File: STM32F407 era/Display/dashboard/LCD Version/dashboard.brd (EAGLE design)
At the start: 200 x 75.1 mm, 61 parts, among them U1 CAT4238TD-GT3

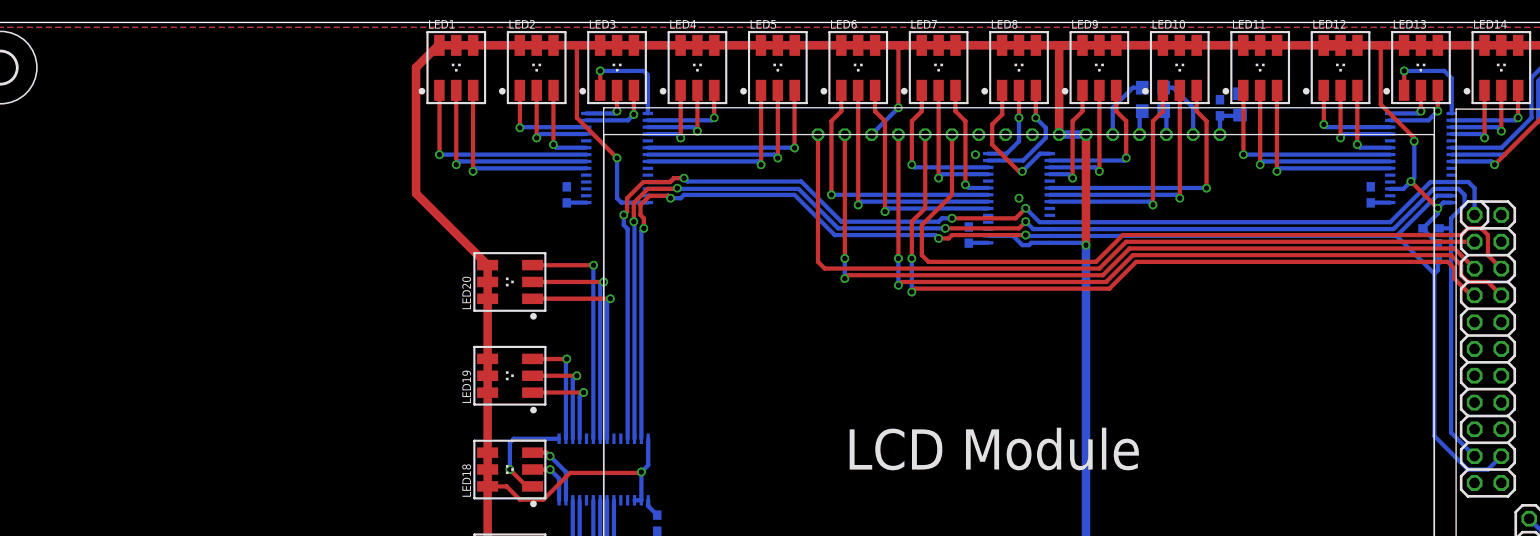
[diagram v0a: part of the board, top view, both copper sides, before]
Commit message: added dashboard control buttons
added buttons to add functionality to the LCD panel
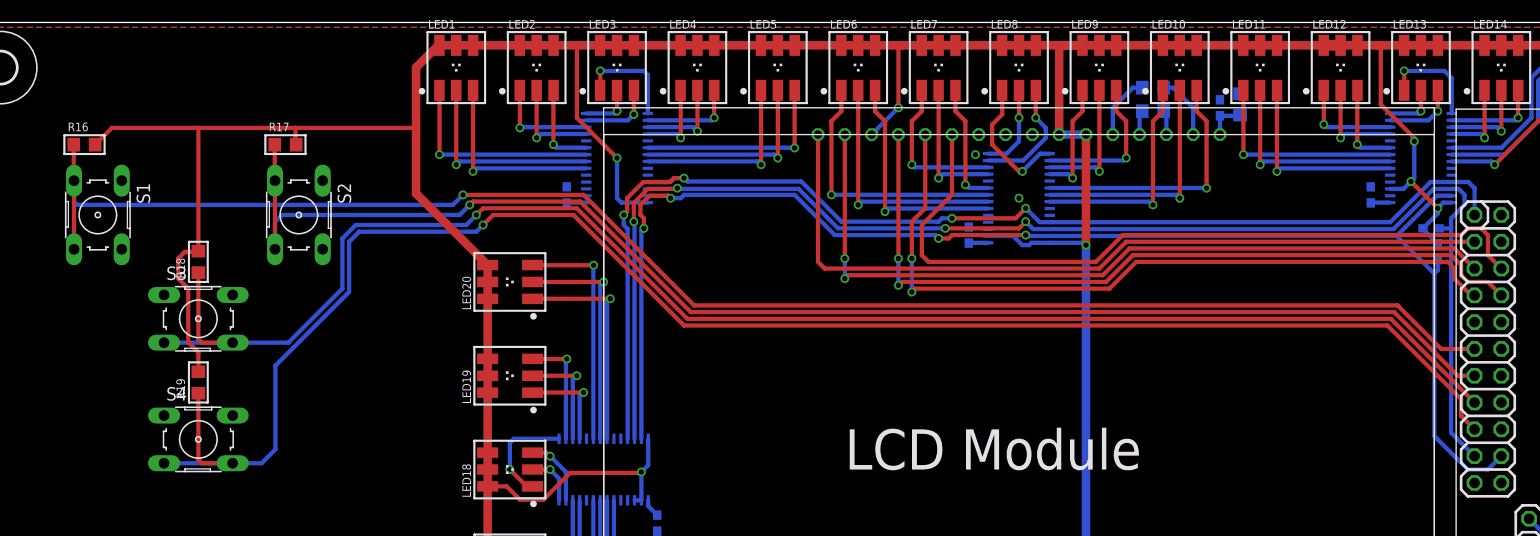
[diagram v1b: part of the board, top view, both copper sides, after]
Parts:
- added R16, R17, R18, R19: 500, microbuilder:_0805
- added S1, S2, S3, S4: (no value), switch-omron:B3F-10XX
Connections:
- new net SW1: R16.1, S1.3, S1.4, U$1.P$11
- new net SW2: R17.1, S2.3, S2.4, U$1.P$13
- new net SW3: R18.1, S3.3, S3.4, U$1.P$15
- new net SW4: R19.1, S4.3, S4.4, U$1.P$17
- net 3.3V: now also R16.2, R17.2, R18.2, R19.2
- net GND: now also S1.1, S1.2, S2.1, S2.2, S3.1, S3.2, S4.1, S4.2
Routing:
- net SW4: track 0.00 -> 160.5 mm, vias 0 -> 1
- net SW1: track 0.00 -> 151.3 mm, vias 0 -> 1
- net SW3: track 0.00 -> 149.6 mm, vias 0 -> 1
- net SW2: track 0.00 -> 133.9 mm, vias 0 -> 1
- net 3.3V: track 469.0 -> 527.1 mm

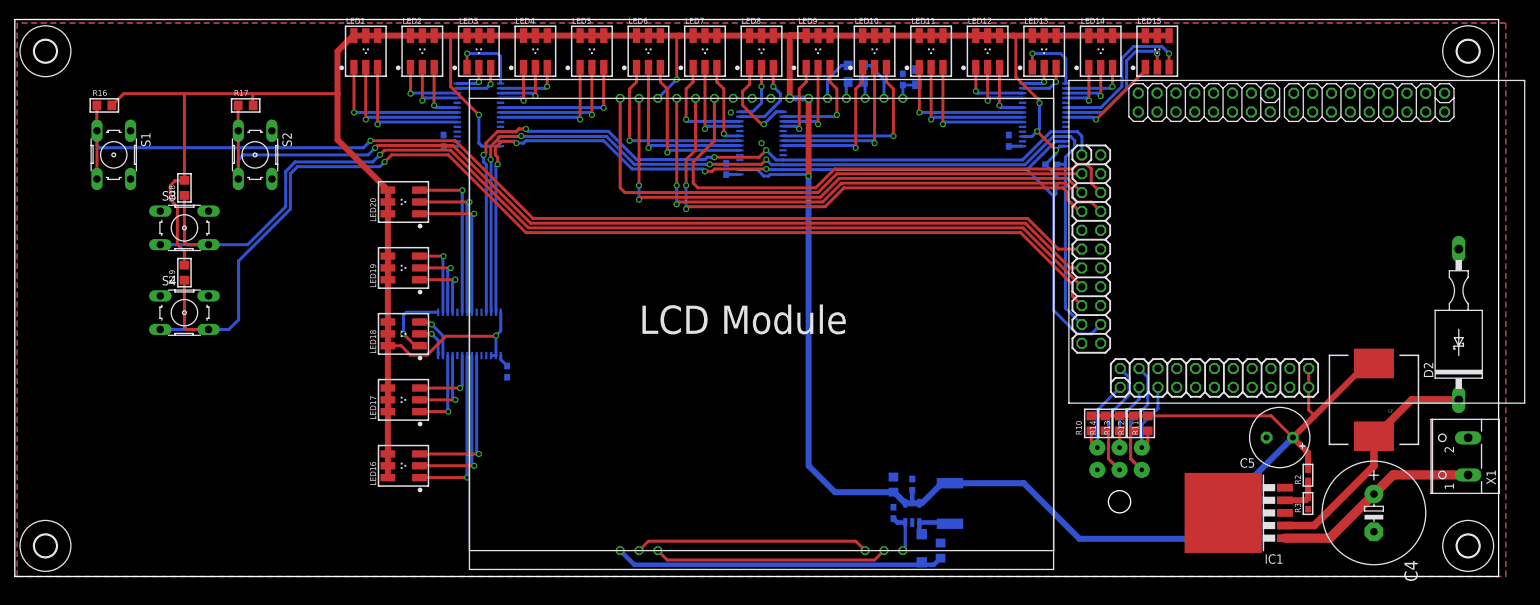
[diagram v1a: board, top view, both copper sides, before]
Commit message: added hardware debounce circuit to buttons
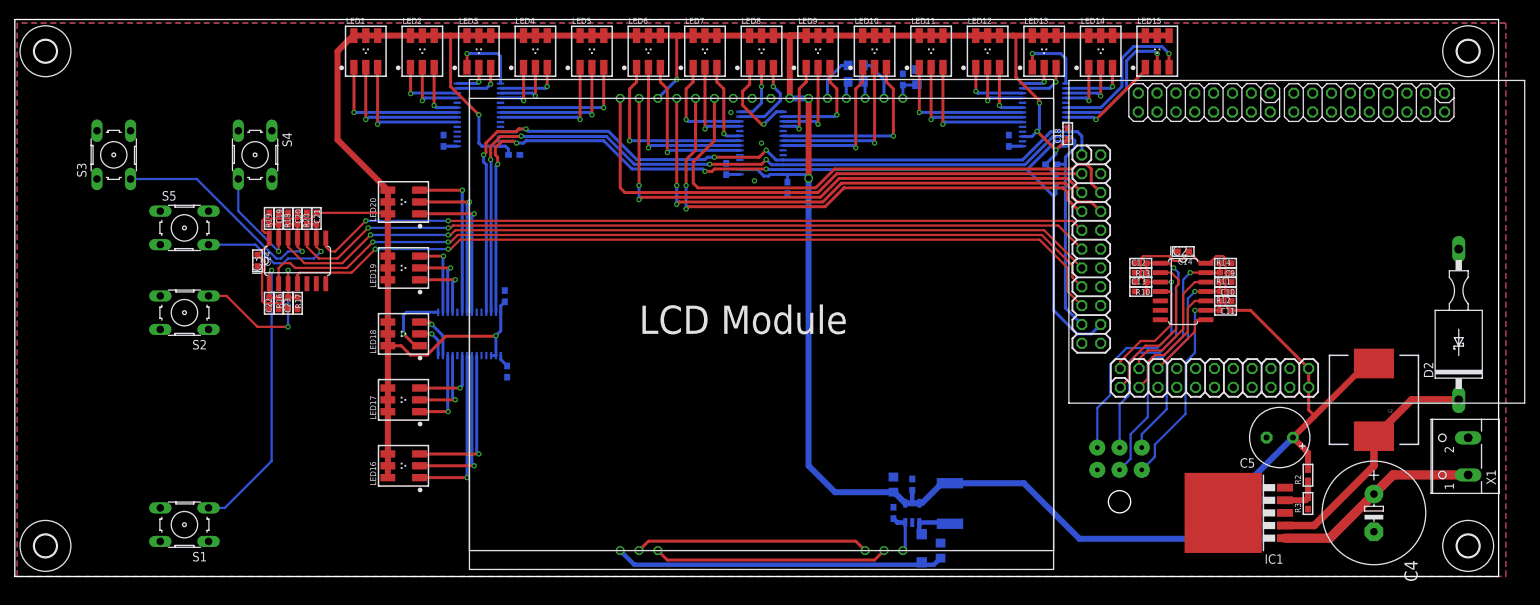
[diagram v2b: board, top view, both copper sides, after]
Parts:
- added C10, C11, C12, C13, C14, C15, C16, C17, C18, C19, C20, C21, C22, C23, C24, C9: 100n, microbuilder:_0603
- added IC2, IC3: 74HC14D, 74xx-eu:SO14
- added R20: 500, microbuilder:_0603
- added S5: (no value), switch-omron:B3F-10XX
- R10, R11, R12, R13, R14, R16, R17, R18, R19: device microbuilder:_0805 -> microbuilder:_0603
- moved S1 50.7 mm to (22.5, 6.03), turned to 180 degrees
- moved R16 34.7 mm to (34.0, 35.9), turned to 270 degrees
- moved R17 27.3 mm to (36.5, 35.9), turned to 270 degrees
- moved R14 26.0 mm to (162.9, 40.0), turned to 0 degrees
- moved S2 23.3 mm to (22.5, 34.6), turned to 180 degrees
- moved S4 23.3 mm to (32.1, 55.9), turned to 270 degrees
- moved R13 21.8 mm to (151.4, 41.3), turned to 180 degrees
- moved R11 20.6 mm to (162.9, 37.5), turned to 0 degrees
- moved R10 20.2 mm to (151.4, 38.7), turned to 180 degrees
- moved R12 19.6 mm to (162.9, 34.9), turned to 0 degrees
- moved R18 15.8 mm to (37.8, 47.3)
- moved R19 14.6 mm to (35.2, 47.3)
- moved S3 13.7 mm to (13.0, 55.9), turned to 90 degrees
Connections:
- new net BTN1S: IC2.2, U$1.P$23
- new net BTN2S: IC2.4, U$1.P$24
- new net BTN3S: IC2.10, U$1.P$25
- new net BTN4S: IC2.12, U$1.P$26
- new net BTN5S: IC2.8, U$1.P$28
- new net SW1S: IC3.2, U$1.P$15
- new net SW2S: IC3.4, U$1.P$17
- new net SW3S: IC3.10, U$1.P$11
- new net SW4S: IC3.12, U$1.P$13
- new net SW5: C21.2, IC3.9, R20.1, S5.3, S5.4
- new net SW5S: IC3.8, U$1.P$9
- net 3.3V: now also C14.1, C15.1, C16.1, C17.1, C18.1, C24.1, IC2.14, IC3.14, R20.2
- net BTN1: now also C12.2, IC2.1, R13.1, U$42.PIN4; no longer R10.1, U$1.P$23, U$42.PIN2
- net BTN2: now also C13.2, IC2.3, R10.1, U$42.PIN2; no longer R14.1, U$1.P$24, U$42.PIN3
- net BTN3: now also C10.2, IC2.11, R11.1, U$42.PIN6; no longer R13.1, U$1.P$25, U$42.PIN4
- net BTN4: now also C9.2, IC2.13, R14.1, U$42.PIN3; no longer R12.1, U$1.P$26, U$42.PIN5
- net BTN5: now also C11.2, IC2.9, R12.1, U$42.PIN5; no longer R11.1, U$1.P$27, U$42.PIN6
- net GND: now also C10.1, C11.1, C12.1, C13.1, C14.2, C15.2, C16.2, C17.2, C18.2, C19.1, C20.1, C21.1, C22.1, C23.1, C24.2, C9.1, IC2.5, IC2.7, IC3.5, IC3.7, S5.1, S5.2
- net SW1: now also C22.2, IC3.1; no longer U$1.P$11
- net SW2: now also C23.2, IC3.3; no longer U$1.P$13
- net SW3: now also C20.2, IC3.11; no longer U$1.P$15
- net SW4: now also C19.2, IC3.13; no longer U$1.P$17
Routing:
- net SW4: track 160.5 -> 17.0 mm
- net SW1S: track 0.00 -> 116.6 mm, vias 0 -> 2
- net SW3: track 149.6 -> 33.2 mm
- net SW2S: track 0.00 -> 114.4 mm, vias 0 -> 2
- net SW4S: track 0.00 -> 113.0 mm, vias 0 -> 2
- net SW3S: track 0.00 -> 109.4 mm, vias 0 -> 2
- net SW1: track 151.3 -> 41.9 mm
- net SW2: track 133.9 -> 25.0 mm, vias 1 -> 2
- net SW5S: track 0.00 -> 105.6 mm, vias 0 -> 2
- net BTN1: track 12.0 -> 34.7 mm, vias 0 -> 1
- net SW5: track 0.00 -> 22.1 mm, vias 0 -> 1
- net BTN1S: track 0.00 -> 21.7 mm
- net BTN5: track 11.6 -> 29.1 mm, vias 0 -> 1
- net BTN4S: track 0.00 -> 17.4 mm
- net BTN3: track 11.5 -> 28.6 mm, vias 0 -> 1
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
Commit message: small cosmic changes
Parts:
- moved S1 24.4 mm to (22.9, 30.5), turned to 0 degrees
- moved S5 15.9 mm to (22.9, 61.9)
- moved S2 10.8 mm to (22.9, 45.4), turned to 0 degrees
- moved S3 2.73 mm to (14.6, 53.7)
- moved S4 2.42 mm to (31.1, 53.7)
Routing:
- net SW5: track 22.1 -> 39.8 mm
- net SW1: track 41.9 -> 28.5 mm
- net SW4: track 17.0 -> 21.6 mm
- net SW3: track 33.2 -> 37.2 mm
- net SW2: track 25.0 -> 23.0 mm, vias 2 -> 1
